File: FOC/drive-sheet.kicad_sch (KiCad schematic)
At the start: 1 part, among them U2 DRV8311H

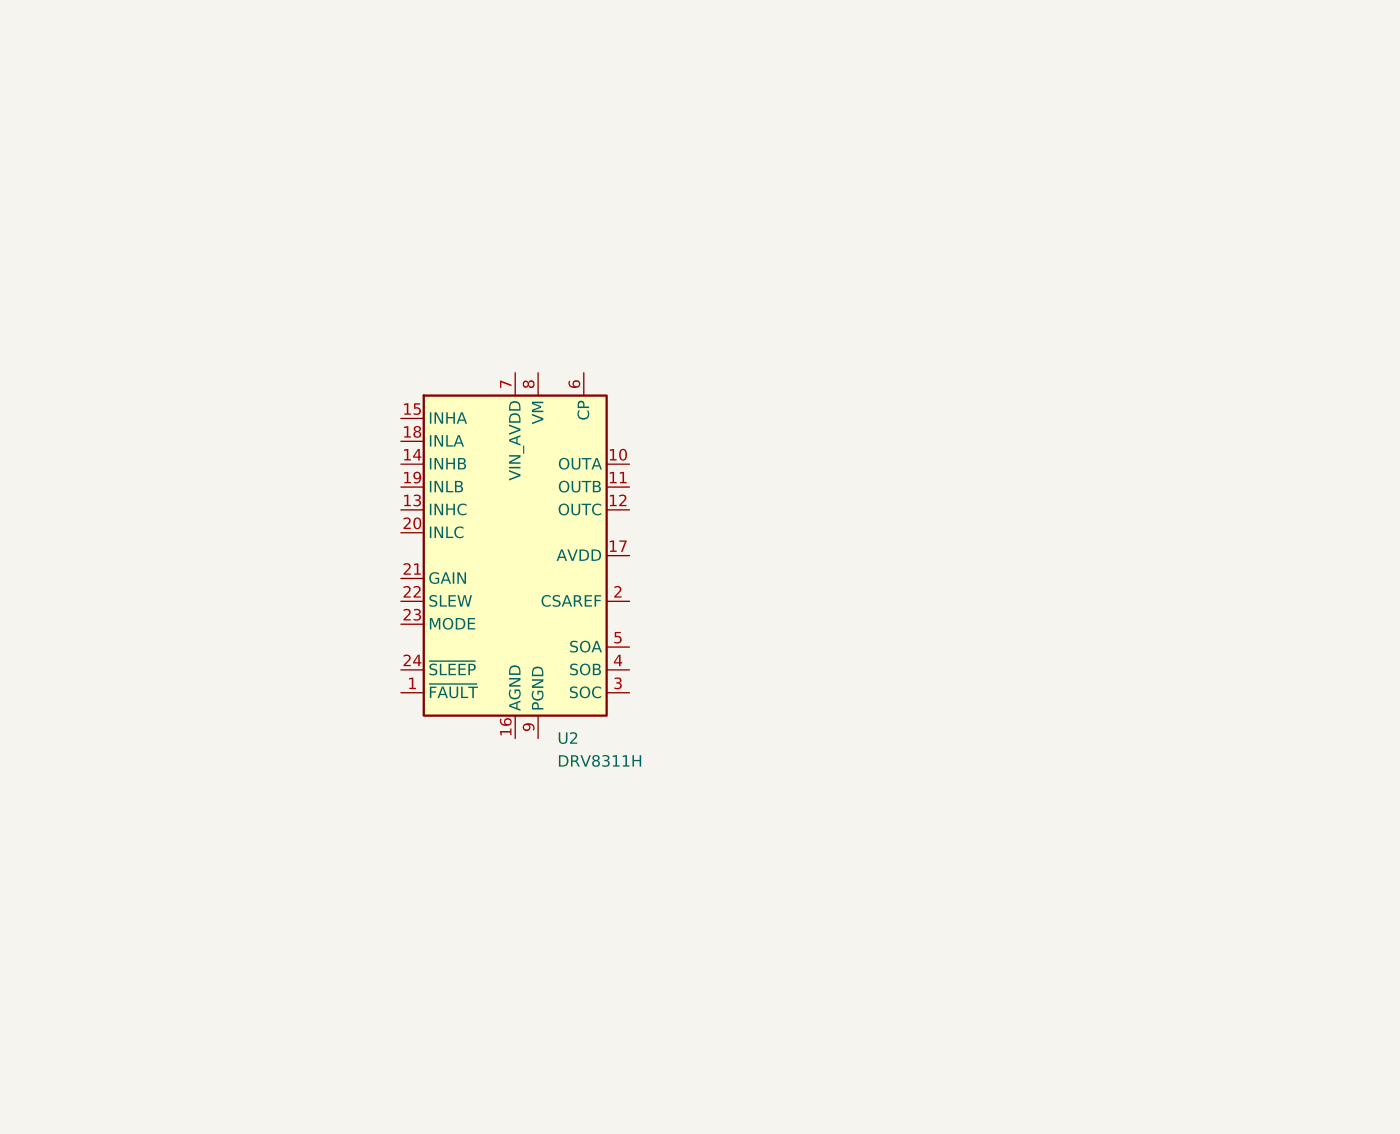
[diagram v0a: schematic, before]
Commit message: CAN + UART done;driver controller done
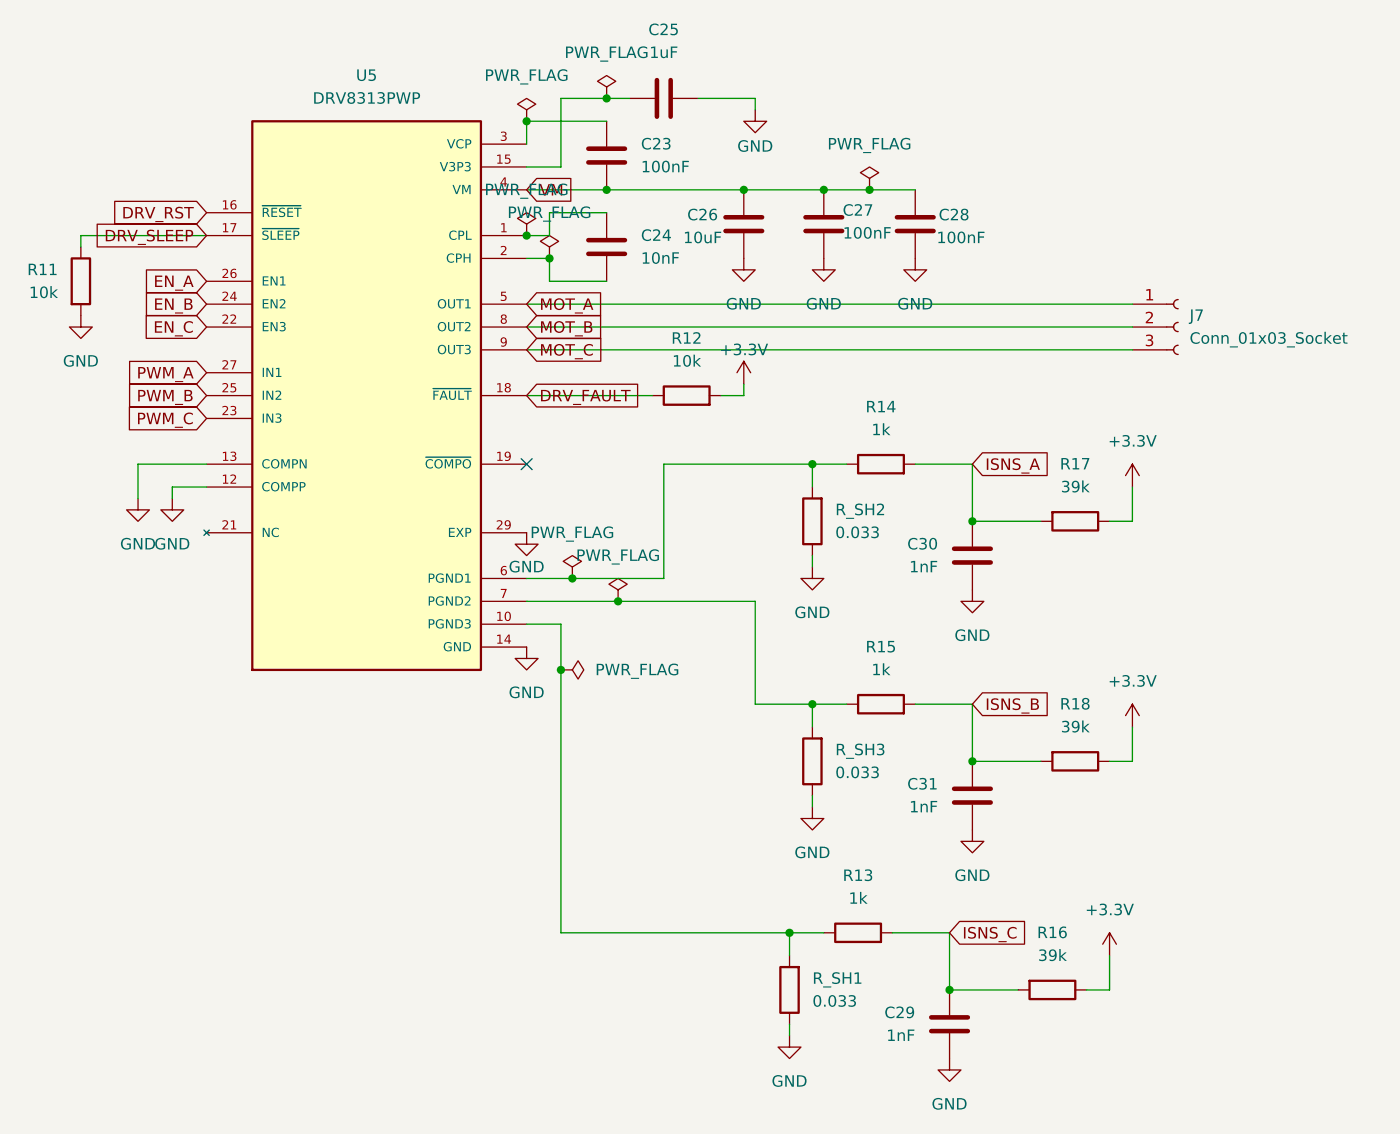
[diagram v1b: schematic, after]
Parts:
- removed U2: DRV8311H, Package_DFN_QFN:Texas_RRW0024A_WQFN-24-1EP_3x3mm_P0.4mm_EP1.9x1.9mm, symbol Driver_Motor:DRV8311H
- added C23, C27, C28: 100nF, Capacitor_SMD:C_0603_1608Metric, symbol Device:C
- added C24: 10nF, Capacitor_SMD:C_0603_1608Metric, symbol Device:C
- added C25: 1uF, Capacitor_SMD:C_0603_1608Metric, symbol Device:C
- added C26: 10uF, Capacitor_SMD:C_0603_1608Metric, symbol Device:C
- added C29, C30, C31: 1nF, Capacitor_SMD:C_0603_1608Metric, symbol Device:C
- added J7: Conn_01x03_Socket, TerminalBlock_MetzConnect:TerminalBlock_MetzConnect_Type101_RT01603HBWC_1x03_P5.08mm_Horizontal, symbol Connector:Conn_01x03_Socket
- added R11, R12: 10k, Resistor_SMD:R_0603_1608Metric, symbol Device:R
- added R13, R14, R15: 1k, Resistor_SMD:R_0603_1608Metric, symbol Device:R
- added R16, R17, R18: 39k, Resistor_SMD:R_0603_1608Metric, symbol Device:R
- added R_SH1, R_SH2, R_SH3: 0.033, Resistor_SMD:R_2512_6332Metric, symbol Device:R
- added U5: DRV8313PWP, DRV8313PWP (1):SOP65P640X120-29N, symbol DRV8313PWP:DRV8313PWP
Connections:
- new net: R14.1, R_SH2.2, U5.6 (PGND1)
- new net: R13.1, R_SH1.2, U5.10 (PGND3)
- new net: R15.1, R_SH3.2, U5.7 (PGND2)
- new net: C24.1, U5.1 (CPL)
- new net: C25.1, U5.15 (V3P3)
- new net: C24.2, U5.2 (CPH)
- new net: C23.1, U5.3 (VCP)
- new net +3.3V: R12.2, R16.1, R17.1, R18.1
- new net DRV_FAULT: R12.1, U5.18 (~{FAULT})
- new net DRV_RST: U5.16 (~{RESET})
- new net DRV_SLEEP: R11.1, U5.17 (~{SLEEP})
- new net EN_A: U5.26 (EN1)
- new net EN_B: U5.24 (EN2)
- new net EN_C: U5.22 (EN3)
- new net GND: C25.2, C26.1, C27.1, C28.1, C29.2, C30.2, C31.2, R11.2, R_SH1.1, R_SH2.1, R_SH3.1, U5.12 (COMPP), U5.13 (COMPN), U5.14 (GND), U5.20 (GND), U5.28 (GND), U5.29 (EXP)
- new net ISNS_A: C30.1, R14.2, R17.2
- new net ISNS_B: C31.1, R15.2, R18.2
- new net ISNS_C: C29.1, R13.2, R16.2
- new net MOT_A: J7.1 (Pin_1), U5.5 (OUT1)
- new net MOT_B: J7.2 (Pin_2), U5.8 (OUT2)
- new net MOT_C: J7.3 (Pin_3), U5.9 (OUT3)
- new net PWM_A: U5.27 (IN1)
- new net PWM_B: U5.25 (IN2)
- new net PWM_C: U5.23 (IN3)
- new net VM: C23.2, C26.2, C27.2, C28.2, U5.11 (VM), U5.4 (VM)
- no-connect marks 0 -> 1

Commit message: drc erc clean; ready to order
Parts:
- removed C26: 10uF, Capacitor_SMD:C_0603_1608Metric, symbol Device:C
- R12: value 10k -> 1k
